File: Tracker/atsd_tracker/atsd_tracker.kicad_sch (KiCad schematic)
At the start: 55 parts, among them J101 ICSP, J102 Battery, J103 SMA_PCB, J104 5V Connector, Q101 IRLML2244, U101 MCP73821_2_SOT-23-5, U102 AZ1117CR-X.XTRG1, U103 DSPIC33CK64MC105, U104 AX5243, X101 16MHz, X102 8MHz

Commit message: Schematic done starting layout
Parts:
- removed U102: AZ1117CR-X.XTRG1, SOT:SOT-89-3, symbol AZ1117:AZ1117CR-X.XTRG1
- added C121, C122: 10pF, SM0402, symbol passives:CAP_0402
- added D103: RED, General_SMD:LED-0603, symbol passives:LED
- added D104: BLUE, General_SMD:LED-0603, symbol passives:LED
- added D105: GREEN, General_SMD:LED-0603, symbol passives:LED
- added J103: Left side, Connector_PinHeader_1.27mm:PinHeader_2x05_P1.27mm_Vertical, symbol Connector_Generic:Conn_02x05_Odd_Even
- added J104: Right side, Connector_PinHeader_1.27mm:PinHeader_2x05_P1.27mm_Vertical, symbol Connector_Generic:Conn_02x05_Odd_Even
- added J106: SMA_PCB, Connectors_RF:SMA_RA_PCB_Amphenol, symbol RF_Connectors:SMA_PCB
- added L103: NC, SM0402, symbol passives:IND_0402
- added L107: IND_0402, SM0402, symbol passives:IND_0402
- added R103, R104, R105, R106, R107, R108, R110, R111, R112, R113, R114, R115: 100, SM0402, symbol passives:RES_0402
- added R118: 10, SM0402, symbol passives:RES_0402
- added R119, R126, R127, R128: NC, SM0402, symbol passives:RES_0402
- added R120, R121, R122: 330, SM0402, symbol passives:RES_0402
- added R125: 10R, SM0402, symbol passives:RES_0402
- added TP101, TP102, TP103, TP104: TP1, Mounting_Holes:3.1mm_Plated, symbol testpoints:TP1
- added U102: XC6209F332MR-G, SOT:SOT25-5, symbol XC6209:XC6209F332MR-G
- added U105: MAX-M8, UBlox:MAX-M8, symbol UBlox:MAX-M8
- C108: renamed from C106; footprint SM0603 -> SM0402; symbol passives:CAP_0603 -> passives:CAP_0402
- C109: renamed from C107; footprint SM0603 -> SM0402; symbol passives:CAP_0603 -> passives:CAP_0402
- C110: renamed from C108; footprint SM0603 -> SM0402; symbol passives:CAP_0603 -> passives:CAP_0402
- C111: renamed from C109; footprint SM0603 -> SM0402; symbol passives:CAP_0603 -> passives:CAP_0402
- C112: renamed from C110; footprint SM0603 -> SM0402; symbol passives:CAP_0603 -> passives:CAP_0402
- J101: renamed from J104; footprint (none) -> Connector_JST:JST_XH_B2B-XH-A_1x02_P2.50mm_Vertical
- R123: renamed from R106; footprint SM0603 -> SM0402; symbol passives:RES_0603 -> passives:RES_0402
- R124: renamed from R107; footprint SM0603 -> SM0402; symbol passives:RES_0603 -> passives:RES_0402
- renumbered C126 to C106, C127 to C107, C111 to C113, C112 to C114, C113 to C115, C114 to C116, C115 to C117, C116 to C118, C117 to C119, C118 to C120, C119 to C123, C120 to C124, C121 to C125, C122 to C126, C123 to C127, C124 to C128, C125 to C129, J103 to J105, J101 to J107, L103 to L104, L104 to L105, L105 to L106, L106 to L108, L107 to L109, L108 to L110, R103 to R109, R104 to R116, R105 to R117, U104 to U106, X102 to X101, X101 to X102
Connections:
- net +3V3: now also J103.1 (Pin_1), J104.1 (Pin_1), R127.2, R128.2, U102.5 (Vout), U105.6 (VBKP), U105.7 (VCCIO), U105.8 (VCC)
- net BMON: now also U103.12 (RA4)
- net GND: now also C122.1, D103.K, D104.K, D105.K, J103.10 (Pin_10), J103.9 (Pin_9), J104.10 (Pin_10), J104.9 (Pin_9), J106.2, L103.2, R119.1, R126.1, TP101.1, TP102.1, TP103.1, TP104.1, U102.2 (Vss), U105.1 (GND), U105.10 (GND), U105.12 (GND)
- net VCC: now also J103.2 (Pin_2), J104.2 (Pin_2), R118.1, U102.1 (Vin)
- net at C117.2, L102.2, L105.1: now also L103.1
- net GPS_WAKE: now reaches U103.1 (RB14)
- net GPS_WAKE: now also U105.5 (EXTINT)
- net left_4: now reaches U103.10 (RA2)
- net left_4: now also R104.1
- net left_5: now reaches U103.11 (RA3)
- net left_5: now also R105.1
- net right_0: now reaches U103.16 (RC2)
- net right_0: now also R113.1
- net right_1: now reaches U103.17 (RC6)
- net right_1: now also R114.1
- net GPS_PPS: now reaches U103.2 (RB15)
- net GPS_PPS: now also U105.4 (PPS)
- net right_2: now reaches U103.20 (RC3)
- net right_2: now also R115.1
- net right_3: now reaches U103.23 (RD10)
- net right_3: now also R106.1
- net right_4: now reaches U103.24 (RC7)
- net right_4: now also R107.1
- net right_5: now reaches U103.25 (RB2)
- net right_5: now also R108.1
- net GPS_RXD: now reaches U103.3 (RC12)
- net GPS_RXD: now also U105.3 (RXD)
- net GPS_SCL: now reaches U103.36 (RB8)
- net GPS_SCL: now also R128.1, U105.17 (SCL)
- net GPS_SDA: now reaches U103.37 (RB9)
- net GPS_SDA: now also R127.1, U105.16 (SDA)
- net GPS_TXD: now reaches U103.4 (RC13)
- net GPS_TXD: now also U105.2 (TXD)
- net at U103.46 (RB11): now also R120.1
- net at U103.47 (RB12): now also R121.1
- net at U103.48 (RB13): now also R122.1
- net left_0: now reaches U103.6 (RD13)
- net left_0: now also R110.1
- net left_1: now reaches U103.7 (RC0)
- net left_1: now also R111.1
- net left_2: now reaches U103.8 (RA0)
- net left_2: now also R112.1
- net left_3: now reaches U103.9 (RA1)
- net left_3: now also R103.1
- new net: J104.8 (Pin_8), R115.2
- new net: C121.1, U105.11 (RF_IN)
- new net: C121.2, J106.1 (sig), L107.1
- new net: J103.8 (Pin_8), R112.2
- new net: J103.4 (Pin_4), R110.2
- new net: D103.A, R120.2
- new net: R118.2, R119.2, U102.3 (CE)
- new net: R125.2, U105.14 (VCC_RF)
- new net: R126.2, U105.18 (~{SFBOOT})
- new net: J103.6 (Pin_6), R111.2
- new net: J104.4 (Pin_4), R113.2
- new net: C122.2, L107.2, R125.1
- new net: D105.A, R122.2
- new net: J104.7 (Pin_7), R108.2
- new net: J103.7 (Pin_7), R105.2
- new net: J103.3 (Pin_3), R103.2
- new net: J103.5 (Pin_5), R104.2
- new net: J104.5 (Pin_5), R107.2
- new net: D104.A, R121.2
- new net: J104.3 (Pin_3), R106.2
- new net: J104.6 (Pin_6), R114.2
- new net GPS_~{RST}: U105.9 (~{RST})
- no-connect marks 3 -> 5
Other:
- note added: "Worst case naked board => 255mW dissipation About 42°C temperature rise. Max 600mW @ 25°C / 240mW @ 85°C Iq = 50uA To be replaced by a SMPS"

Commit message: Produced prototype
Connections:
- net GPS_~{RST}: now also U103.48 (RB13)
- net left_3: now also U103.40 (RC10); no longer U103.9 (RA1)
- net left_4: now also U103.39 (RC5); no longer U103.10 (RA2)
- net left_5: now also U103.38 (RC4); no longer U103.11 (RA3)
- net R2_P: now reaches C117.2, L102.2, L103.1, L105.1
- net R0_P: now reaches C119.1, C123.2, L108.2, U106.3 (ANTP)
- net R0_N: now reaches C120.1, C124.2, L109.2, U106.4 (ANTN)
- net R2_N: now reaches C116.1, C118.2, L104.2, L106.1
- net R1_P: now reaches C119.2, L105.2
- net at R122.1: now also U103.47 (RB12); no longer U103.48 (RB13)
- net at U103.45 (RB10): now also R120.1
- net at U103.46 (RB11): now also R121.1; no longer R120.1
- net R1_N: now reaches C120.2, L106.2
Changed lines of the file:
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@@
     (stroke (width 0) (type default) (color 0 0 0 0))
   )
-  (wire (pts (xy 198.755 94.615) (xy 198.755 88.265))
-    (stroke (width 0) (type default) (color 0 0 0 0))
-  )
   (wire (pts (xy 73.025 53.975) (xy 69.85 53.975))
     (stroke (width 0) (type default) (color 0 0 0 0))
@@
     (stroke (width 0) (type default) (color 0 0 0 0))
   )
-  (wire (pts (xy 198.12 68.58) (xy 202.565 68.58))
-    (stroke (width 0) (type default) (color 0 0 0 0))
-  )
   (wire (pts (xy 226.695 66.675) (xy 220.98 66.675))
     (stroke (width 0) (type default) (color 0 0 0 0))
@@
     (stroke (width 0) (type default) (color 0 0 0 0))
   )
-  (wire (pts (xy 200.025 98.425) (xy 200.025 89.535))
-    (stroke (width 0) (type default) (color 0 0 0 0))
-  )
   (wire (pts (xy 214.63 58.42) (xy 214.63 55.88))
     (stroke (width 0) (type default) (color 0 0 0 0))
@@
     (stroke (width 0) (type default) (color 0 0 0 0))
   )
-  (wire (pts (xy 197.485 90.805) (xy 197.485 86.995))
-    (stroke (width 0) (type default) (color 0 0 0 0))
-  )
   (wire (pts (xy 247.015 62.865) (xy 247.015 64.135))
     (stroke (width 0) (type default) (color 0 0 0 0))
   )
-  (wire (pts (xy 200.025 89.535) (xy 202.565 89.535))
-    (stroke (width 0) (type default) (color 0 0 0 0))
-  )
   (wire (pts (xy 335.28 86.995) (xy 335.28 85.725))
     (stroke (width 0) (type default) (color 0 0 0 0))
@@
     (stroke (width 0) (type default) (color 0 0 0 0))
   )
-  (wire (pts (xy 193.675 98.425) (xy 200.025 98.425))
+  (wire (pts (xy 193.675 98.425) (xy 196.85 98.425))
     (stroke (width 0) (type default) (color 0 0 0 0))
   )
@@
     (stroke (width 0) (type default) (color 0 0 0 0))
   )
+  (wire (pts (xy 220.98 70.485) (xy 226.695 70.485))
+    (stroke (width 0) (type default) (color 0 0 0 0))
+  )
   (wire (pts (xy 334.01 136.525) (xy 337.185 136.525))
     (stroke (width 0) (type default) (color 0 0 0 0))
@@
     (stroke (width 0) (type default) (color 0 0 0 0))
   )
-  (wire (pts (xy 198.755 88.265) (xy 202.565 88.265))
-    (stroke (width 0) (type default) (color 0 0 0 0))
-  )
   (wire (pts (xy 208.915 95.885) (xy 208.915 99.06))
     (stroke (width 0) (type default) (color 0 0 0 0))
@@
     (stroke (width 0) (type default) (color 0 0 0 0))
   )
+  (wire (pts (xy 196.85 88.265) (xy 196.85 98.425))
+    (stroke (width 0) (type default) (color 0 0 0 0))
+  )
   (wire (pts (xy 43.815 54.61) (xy 43.815 55.88))
     (stroke (width 0) (type default) (color 0 0 0 0))
@@
     (stroke (width 0) (type default) (color 0 0 0 0))
   )
-  (wire (pts (xy 197.485 86.995) (xy 202.565 86.995))
-    (stroke (width 0) (type default) (color 0 0 0 0))
-  )
   (wire (pts (xy 313.69 135.255) (xy 313.69 136.525))
     (stroke (width 0) (type default) (color 0 0 0 0))
@@
     (stroke (width 0) (type default) (color 0 0 0 0))
   )
+  (wire (pts (xy 220.98 78.105) (xy 226.695 78.105))
+    (stroke (width 0) (type default) (color 0 0 0 0))
+  )
   (wire (pts (xy 357.505 152.4) (xy 345.44 152.4))
     (stroke (width 0) (type default) (color 0 0 0 0))
@@
     (stroke (width 0) (type default) (color 0 0 0 0))
   )
-  (wire (pts (xy 193.675 90.805) (xy 197.485 90.805))
+  (wire (pts (xy 193.675 90.805) (xy 195.58 90.805))
     (stroke (width 0) (type default) (color 0 0 0 0))
   )
@@
     (stroke (width 0) (type default) (color 0 0 0 0))
   )
+  (wire (pts (xy 198.12 89.535) (xy 202.565 89.535))
+    (stroke (width 0) (type default) (color 0 0 0 0))
+  )
   (wire (pts (xy 357.505 147.955) (xy 357.505 152.4))
     (stroke (width 0) (type default) (color 0 0 0 0))
   )
+  (wire (pts (xy 202.565 88.265) (xy 196.85 88.265))
+    (stroke (width 0) (type default) (color 0 0 0 0))
+  )
   (wire (pts (xy 210.82 58.42) (xy 210.82 55.88))
     (stroke (width 0) (type default) (color 0 0 0 0))
@@
     (stroke (width 0) (type default) (color 0 0 0 0))
   )
-  (wire (pts (xy 198.12 69.85) (xy 202.565 69.85))
-    (stroke (width 0) (type default) (color 0 0 0 0))
-  )
   (wire (pts (xy 194.31 80.645) (xy 202.565 80.645))
     (stroke (width 0) (type default) (color 0 0 0 0))
@@
     (stroke (width 0) (type default) (color 0 0 0 0))
   )
+  (wire (pts (xy 196.215 86.995) (xy 196.215 94.615))
+    (stroke (width 0) (type default) (color 0 0 0 0))
+  )
   (wire (pts (xy 85.725 49.53) (xy 85.725 50.8))
     (stroke (width 0) (type default) (color 0 0 0 0))
@@
     (stroke (width 0) (type default) (color 0 0 0 0))
   )
+  (wire (pts (xy 220.98 71.755) (xy 226.695 71.755))
+    (stroke (width 0) (type default) (color 0 0 0 0))
+  )
   (wire (pts (xy 354.33 145.415) (xy 357.505 145.415))
     (stroke (width 0) (type default) (color 0 0 0 0))
@@
     (stroke (width 0) (type default) (color 0 0 0 0))
   )
-  (wire (pts (xy 198.12 67.31) (xy 202.565 67.31))
-    (stroke (width 0) (type default) (color 0 0 0 0))
-  )
   (wire (pts (xy 345.44 149.225) (xy 346.71 149.225))
     (stroke (width 0) (type default) (color 0 0 0 0))
@@
     (stroke (width 0) (type default) (color 0 0 0 0))
   )
+  (wire (pts (xy 202.565 85.725) (xy 195.58 85.725))
+    (stroke (width 0) (type default) (color 0 0 0 0))
+  )
   (wire (pts (xy 74.93 161.29) (xy 74.295 161.29))
     (stroke (width 0) (type default) (color 0 0 0 0))
@@
     (stroke (width 0) (type default) (color 0 0 0 0))
   )
+  (wire (pts (xy 195.58 85.725) (xy 195.58 90.805))
+    (stroke (width 0) (type default) (color 0 0 0 0))
+  )
   (wire (pts (xy 93.345 128.905) (xy 99.06 128.905))
     (stroke (width 0) (type default) (color 0 0 0 0))
   )
+  (wire (pts (xy 202.565 86.995) (xy 196.215 86.995))
+    (stroke (width 0) (type default) (color 0 0 0 0))
+  )
   (wire (pts (xy 45.72 67.31) (xy 49.53 67.31))
     (stroke (width 0) (type default) (color 0 0 0 0))
@@
     (stroke (width 0) (type default) (color 0 0 0 0))
   )
-  (wire (pts (xy 193.675 94.615) (xy 198.755 94.615))
+  (wire (pts (xy 193.675 94.615) (xy 196.215 94.615))
     (stroke (width 0) (type default) (color 0 0 0 0))
   )
@@
     (effects (font (size 0.635 0.635)) (justify left bottom))
   )
+  (label "R0_P" (at 351.155 140.97 0)
+    (effects (font (size 1 1)) (justify left bottom))
+  )
   (label "RF_CLK" (at 395.605 144.78 180)
     (effects (font (size 0.635 0.635)) (justify right bottom))
@@
     (effects (font (size 0.635 0.635)) (justify right bottom))
   )
+  (label "GPS_~{RST}" (at 198.12 89.535 0)
+    (effects (font (size 0.635 0.635)) (justify left bottom))
+  )
   (label "RF_MOSI" (at 395.605 142.24 180)
     (effects (font (size 0.635 0.635)) (justify right bottom))
@@
     (effects (font (size 0.635 0.635)) (justify left bottom))
   )
+  (label "R1_N" (at 322.58 144.145 0)
+    (effects (font (size 1 1)) (justify left bottom))
+  )
   (label "RF_IRQ" (at 226.695 66.675 180)
     (effects (font (size 0.635 0.635)) (justify right bottom))
@@
     (effects (font (size 0.635 0.635)) (justify left bottom))
   )
+  (label "left_4" (at 226.695 71.755 180)
+    (effects (font (size 0.635 0.635)) (justify right bottom))
+  )
   (label "~{RF_CS}" (at 194.31 78.105 0)
     (effects (font (size 0.635 0.635)) (justify left bottom))
@@
     (effects (font (size 0.635 0.635)) (justify right bottom))
   )
+  (label "left_5" (at 226.695 70.485 180)
+    (effects (font (size 0.635 0.635)) (justify right bottom))
+  )
+  (label "R2_N" (at 311.15 144.145 0)
+    (effects (font (size 1 1)) (justify left bottom))
+  )
   (label "GPS_WAKE" (at 378.46 85.725 180)
     (effects (font (size 0.635 0.635)) (justify right bottom))
   )
+  (label "R0_N" (at 351.155 143.51 0)
+    (effects (font (size 1 1)) (justify left bottom))
+  )
   (label "~{MCLR}" (at 180.34 62.865 0)
     (effects (font (size 1.27 1.27)) (justify left bottom))
   )
-  (label "left_5" (at 198.12 69.85 0)
-    (effects (font (size 0.635 0.635)) (justify left bottom))
+  (label "R1_P" (at 322.58 136.525 0)
+    (effects (font (size 1 1)) (justify left bottom))
   )
   (label "right_1" (at 226.695 73.025 180)
     (effects (font (size 0.635 0.635)) (justify right bottom))
   )
-  (label "left_4" (at 198.12 68.58 0)
-    (effects (font (size 0.635 0.635)) (justify left bottom))
+  (label "left_3" (at 226.695 78.105 180)
+    (effects (font (size 0.635 0.635)) (justify right bottom))
+  )
+  (label "R2_P" (at 311.15 136.525 0)
+    (effects (font (size 1 1)) (justify left bottom))
   )
   (label "~{RF_CS}" (at 395.605 146.05 180)
     (effects (font (size 0.635 0.635)) (justify right bottom))
   )
-  (label "left_3" (at 198.12 67.31 0)
-    (effects (font (size 0.635 0.635)) (justify left bottom))
-  )
   (label "GPS_PPS" (at 378.46 86.995 180)

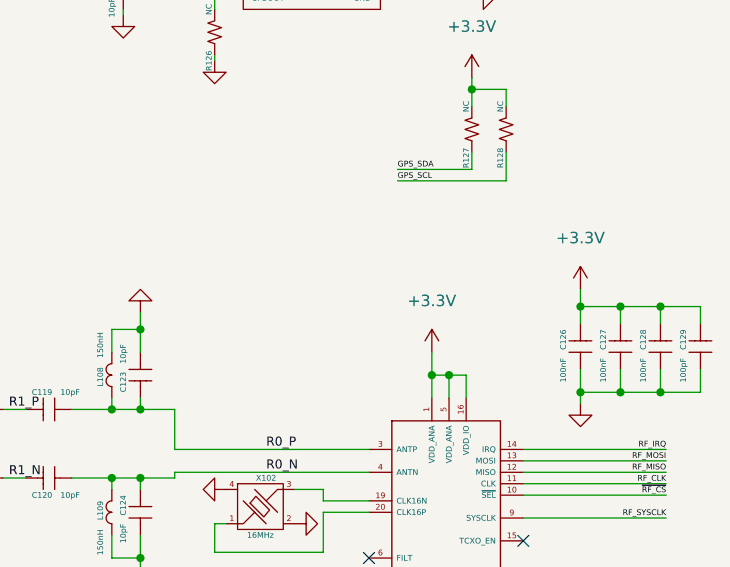
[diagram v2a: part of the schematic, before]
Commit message: OnSemi discontinued AX5043 and all sub-ghz, switching to si446x
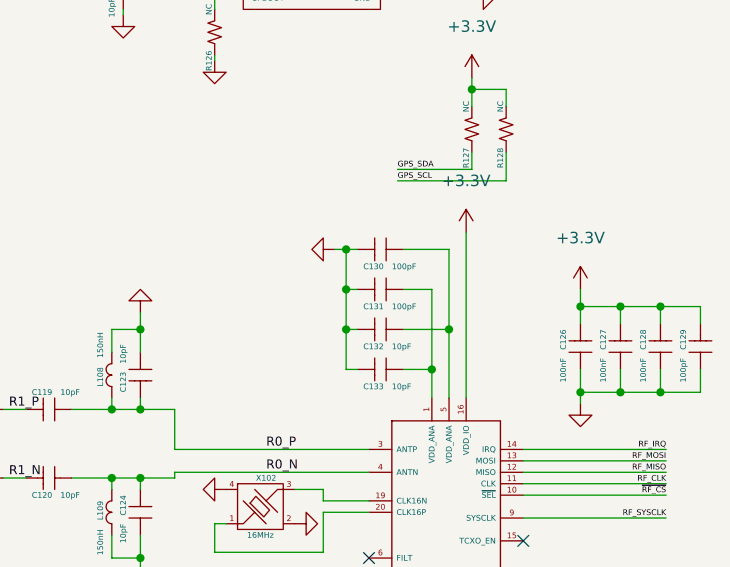
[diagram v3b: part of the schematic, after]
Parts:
- added C130, C131: 100pF, SM0402, symbol passives:CAP_0402
- added C132, C133: 10pF, SM0402, symbol passives:CAP_0402
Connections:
- net +3V3: no longer U106.1 (VDD_ANA), U106.5 (VDD_ANA)
- net GND: now also C130.2, C131.2, C132.2, C133.2
- new net: C130.1, C132.1, U106.5 (VDD_ANA)
- new net: C131.1, C133.1, U106.1 (VDD_ANA)
